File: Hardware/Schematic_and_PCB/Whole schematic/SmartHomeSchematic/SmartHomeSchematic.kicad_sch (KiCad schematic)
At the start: 51 parts, among them J1 PIR_sensor, J2 LCD_display, J3 Power, Q1 BC557, Q3 BC557, Q4 BC557, Q5 BC557, Q6 BC557, Q7 BC557, SW1 Room_1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

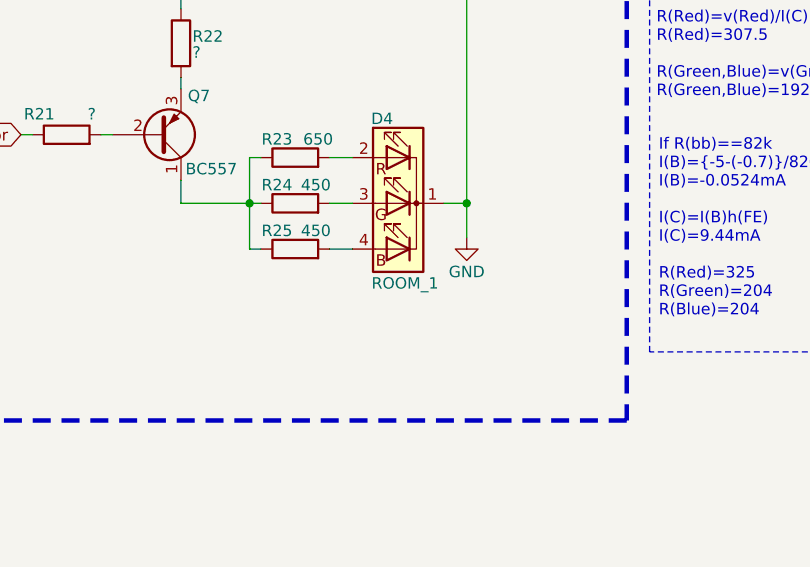
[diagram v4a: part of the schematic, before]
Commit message: Update PCB LCD
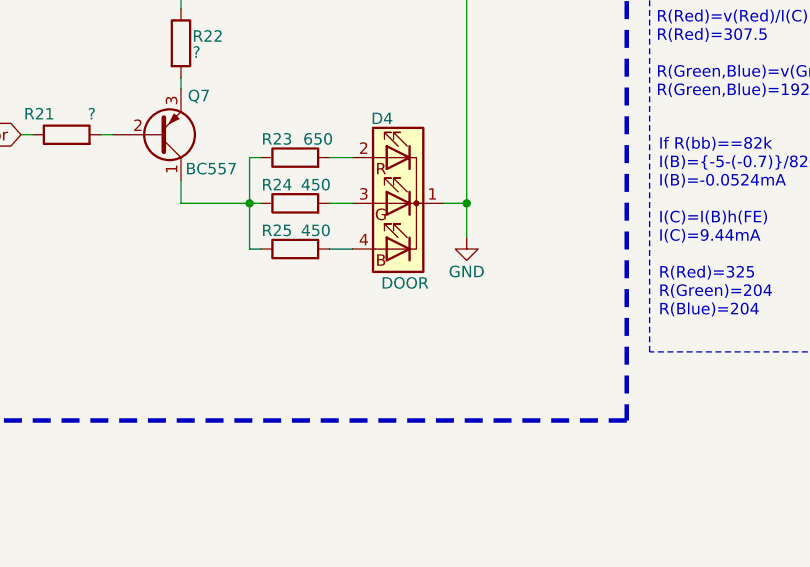
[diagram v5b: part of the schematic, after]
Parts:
- D4: value ROOM_1 -> DOOR
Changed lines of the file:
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@@
 			)
 		)
-		(property "Value" "ROOM_1"
+		(property "Value" "DOOR"
 			(at 325.882 199.39 0)
 			(effects

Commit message: Add room 2 header file.
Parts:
- added H1, H2, H3, H4: MountingHole, symbol Mechanical:MountingHole
- added TP1: TestPoint, symbol Connector:TestPoint
